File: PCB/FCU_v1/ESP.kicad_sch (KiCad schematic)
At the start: 10 parts, among them IC3 ESP32-C3-MINI-1-N4X, SW3 SW_MEC_5G

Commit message: Repaired library
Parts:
- removed IC3: ESP32-C3-MINI-1-N4X, ESP32C3MINI1N4X, symbol SamacSys_Parts:ESP32-C3-MINI-1-N4X
- added IC4: ESP32-C3-MINI-1-N4X, ESP32C3MINI1N4X, symbol SamacSys_Parts:ESP32-C3-MINI-1-N4X
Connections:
- net +3.3V: now also IC4.3 (3V3)
- net GND: now also IC4.1 (GND), IC4.11 (GND_3), IC4.14 (GND_4), IC4.2 (GND_2), IC4.36 (GND_5), IC4.37 (GND_6), IC4.38 (GND_7), IC4.39 (GND_8), IC4.40 (GND_9), IC4.41 (GND_10), IC4.42 (GND_11), IC4.43 (GND_12), IC4.44 (GND_13), IC4.45 (GND_14), IC4.46 (GND_15), IC4.47 (GND_16), IC4.48 (GND_17), IC4.49 (GND_18), IC4.50 (GND_19), IC4.51 (GND_20), IC4.52 (GND_21), IC4.53 (GND_22), IC4.54 (GND_23), IC4.55 (GND_24), IC4.56 (GND_25), IC4.57 (GND_26), IC4.58 (GND_27), IC4.59 (GND_28), IC4.60 (GND_29), IC4.61 (GND_30)
- net UART_RX_ESP_DBG: now also IC4.30 (RXD0)
- net UART_RX_ESP_STM: now also IC4.6 (IO3)
- net UART_TX_ESP_DBG: now also IC4.31 (TXD0)
- net UART_TX_ESP_STM: now also IC4.16 (IO10)
- net at C44.1, R44.1, R45.2: now also IC4.8 (EN)
- net at R46.1: now also IC4.19 (IO5)
- new net: IC4.10 (NC_4), IC4.15 (NC_5), IC4.17 (NC_6), IC4.24 (NC_7), IC4.25 (NC_8), IC4.28 (NC_9), IC4.29 (NC_10), IC4.32 (NC_11), IC4.33 (NC_12), IC4.34 (NC_13), IC4.35 (NC_14), IC4.4 (NC_1), IC4.7 (NC_2), IC4.9 (NC_3)
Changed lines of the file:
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@@
+	)
+	(symbol
+		(lib_id "SamacSys_Parts:ESP32-C3-MINI-1-N4X")
+		(at 76.2 58.42 0)
+		(unit 1)
+		(exclude_from_sim no)
+		(in_bom yes)
+		(on_board yes)
+		(dnp no)
+		(fields_autoplaced yes)
+		(property "Reference" "IC4"
+			(at 94.8533 54.61 0)
+			(effects
+				(font
+					(size 1.27 1.27)
+				)
+				(justify left)
+			)
+		)
+		(property "Value" "ESP32-C3-MINI-1-N4X"
+			(at 94.8533 57.15 0)
+			(effects
+				(font
+					(size 1.27 1.27)
+				)
+				(justify left)
+			)
+		)
+		(property "Footprint" "ESP32C3MINI1N4X"
+			(at 105.41 153.34 0)
+			(effects
+				(font
+					(size 1.27 1.27)
+				)
+				(justify left top)
+				(hide yes)
+			)
+		)
+		(property "Datasheet" "https://documentation.espressif.com/esp32-c3-mini-1_datasheet_en.pdf"
+			(at 105.41 253.34 0)
+			(effects
+				(font
+					(size 1.27 1.27)
+				)
+				(justify left top)
+				(hide yes)
+			)
+		)
+		(property "Description" "Bluetooth, WiFi 802.11b/g/n, Bluetooth v5.0 Transceiver Module 2.4GHz Integrated, Trace Surface Mount , 3V ~ 3.6V , -40C ~ 85C (TA)"
+			(at 76.2 58.42 0)
+			(effects
+				(font
+					(size 1.27 1.27)
+				)
+				(hide yes)
+			)
+		)
+		(property "Height" "2.55"
+			(at 105.41 453.34 0)
+			(effects
+				(font
+					(size 1.27 1.27)
+				)
+				(justify left top)
+				(hide yes)
+			)
+		)
+		(property "Mouser Part Number" ""
+			(at 105.41 553.34 0)
+			(effects
+				(font
+					(size 1.27 1.27)
+				)
+				(justify left top)
+				(hide yes)
+			)
+		)
+		(property "Mouser Price/Stock" ""
+			(at 105.41 653.34 0)
+			(effects
+				(font
+					(size 1.27 1.27)
+				)
+				(justify left top)
+				(hide yes)
+			)
+		)
+		(property "Manufacturer_Name" "Espressif Systems"
+			(at 105.41 753.34 0)
+			(effects
+				(font
+					(size 1.27 1.27)
+				)
+				(justify left top)
+				(hide yes)
+			)
+		)
+		(property "Manufacturer_Part_Number" "ESP32-C3-MINI-1-N4X"
+			(at 105.41 853.34 0)
+			(effects
+				(font
+					(size 1.27 1.27)
+				)
+				(justify left top)
+				(hide yes)
+			)
+		)
+		(pin "18"
+		)
+		(pin "20"
+		)
+		(pin "33"
+		)
+		(pin "13"
+		)
+		(pin "10"
+		)
+		(pin "29"
+		)
+		(pin "16"
+		)
+		(pin "14"
+		)
+		(pin "4"
+		)
+		(pin "34"
+		)
+		(pin "25"
+		)
+		(pin "24"
+		)
+		(pin "28"
+		)
+		(pin "35"
+		)
+		(pin "9"
+		)
+		(pin "6"
+		)
+		(pin "17"
+		)
+		(pin "12"
+		)
+		(pin "32"
+		)
+		(pin "5"
+		)
+		(pin "15"
+		)
+		(pin "7"
+		)
+		(pin "19"
+		)
+		(pin "21"
+		)
+		(pin "22"
+		)
+		(pin "23"
+		)
+		(pin "3"
+		)
+		(pin "1"
+		)
+		(pin "11"
+		)
+		(pin "58"
+		)
+		(pin "36"
+		)
+		(pin "61"
+		)
+		(pin "42"
+		)
+		(pin "43"
+		)
+		(pin "48"
+		)
+		(pin "40"
+		)
+		(pin "2"
+		)
+		(pin "49"
+		)
+		(pin "50"
+		)
+		(pin "37"
+		)
+		(pin "41"
+		)
+		(pin "45"
+		)
+		(pin "52"
+		)
+		(pin "53"
+		)
+		(pin "54"
+		)
+		(pin "44"
+		)
+		(pin "47"
+		)
+		(pin "55"
+		)
+		(pin "51"
+		)
+		(pin "56"
+		)
+		(pin "57"
+		)
+		(pin "39"
+		)
+		(pin "38"
+		)
+		(pin "46"
+		)
+		(pin "59"
+		)
+		(pin "60"
+		)
+		(pin "30"
+		)
+		(pin "31"
+		)
+		(pin "8"
+		)
+		(pin "26"
+		)
+		(pin "27"
+		)
+		(instances
+			(project ""
+				(path "/ace60bf5-8c2a-49e8-98f3-824f03a0dfeb/aae47d4f-fc32-408a-9d63-5fc67cfcb68c"
+					(reference "IC4")
+					(unit 1)
+				)
+			)
+		)
 	)
 	(symbol
@@
 					(unit 1)
 				)
-			)
-		)
-	)
-	(symbol
-		(lib_id "SamacSys_Parts:ESP32-C3-MINI-1-N4X")
-		(at 76.2 58.42 0)
-		(unit 1)
-		(exclude_from_sim no)
-		(in_bom yes)
-		(on_board yes)
-		(dnp no)
-		(property "Reference" "IC3"
-			(at 95.504 57.912 0)
-			(effects
-				(font
-					(size 1.27 1.27)
-				)
-				(justify left)
-			)
-		)
-		(property "Value" "ESP32-C3-MINI-1-N4X"
-			(at 93.98 95.25 0)
-			(effects
-				(font
-					(size 1.27 1.27)
-				)
-				(justify left)
-			)
-		)
-		(property "Footprint" "ESP32C3MINI1N4X"
-			(at 105.41 153.34 0)
-			(effects
-				(font
-					(size 1.27 1.27)
-				)
-				(justify left top)
-				(hide yes)
-			)
-		)
-		(property "Datasheet" "https://documentation.espressif.com/esp32-c3-mini-1_datasheet_en.pdf"
-			(at 105.41 253.34 0)
-			(effects
-				(font
-					(size 1.27 1.27)
-				)
-				(justify left top)
-				(hide yes)
-			)
-		)
-		(property "Description" "Bluetooth, WiFi 802.11b/g/n, Bluetooth v5.0 Transceiver Module 2.4GHz Integrated, Trace Surface Mount , 3V ~ 3.6V , -40C ~ 85C (TA)"
-			(at 76.2 58.42 0)
-			(effects
-				(font
-					(size 1.27 1.27)
-				)
-				(hide yes)
-			)
-		)
-		(property "Height" "2.55"
-			(at 105.41 453.34 0)
-			(effects
-				(font
-					(size 1.27 1.27)
-				)
-				(justify left top)
-				(hide yes)
-			)
-		)
-		(property "Mouser Part Number" ""
-			(at 105.41 553.34 0)
-			(effects
-				(font
-					(size 1.27 1.27)
-				)
-				(justify left top)
-				(hide yes)
-			)
-		)
-		(property "Mouser Price/Stock" ""
-			(at 105.41 653.34 0)
-			(effects
-				(font
-					(size 1.27 1.27)
-				)
-				(justify left top)
-				(hide yes)
-			)
-		)
-		(property "Manufacturer_Name" "Espressif Systems"
-			(at 105.41 753.34 0)
-			(effects
-				(font
-					(size 1.27 1.27)
-				)
-				(justify left top)
-				(hide yes)
-			)
-		)
-		(property "Manufacturer_Part_Number" "ESP32-C3-MINI-1-N4X"
-			(at 105.41 853.34 0)
-			(effects
-				(font
-					(size 1.27 1.27)
-				)
-				(justify left top)
-				(hide yes)
-			)
-		)
-		(pin "14"
-		)
-		(pin "2"
-		)
-		(pin "21"
-		)
-		(pin "16"
-		)
-		(pin "26"
-		)
-		(pin "28"
-		)
-		(pin "15"
-		)
-		(pin "7"
-		)
-		(pin "10"
-		)
-		(pin "1"
-		)
-		(pin "3"
-		)
-		(pin "5"
-		)
-		(pin "6"
-		)
-		(pin "9"
-		)
-		(pin "11"
-		)
-		(pin "8"
-		)
-		(pin "4"
-		)
-		(pin "12"
-		)
-		(pin "13"
-		)
-		(pin "18"
-		)
-		(pin "17"
-		)
-		(pin "19"
-		)
-		(pin "20"
-		)
-		(pin "22"
-		)
-		(pin "23"
-		)
-		(pin "24"
-		)
-		(pin "25"
-		)
-		(pin "27"
-		)
-		(pin "53"
-		)
-		(pin "50"
-		)
-		(pin "31"
-		)
-		(pin "40"
-		)
-		(pin "47"
-		)
-		(pin "37"
-		)
-		(pin "34"
-		)
-		(pin "42"
-		)
-		(pin "46"
-		)
-		(pin "32"
-		)
-		(pin "33"
-		)
-		(pin "35"
-		)
-		(pin "45"
-		)
-		(pin "44"
-		)
-		(pin "49"
-		)
-		(pin "52"
-		)
-		(pin "48"
-		)
-		(pin "39"
-		)
-		(pin "30"
-		)
-		(pin "41"
-		)
-		(pin "29"
-		)
-		(pin "38"
-		)
-		(pin "43"
-		)
-		(pin "36"
-		)
-		(pin "51"
-		)
-		(pin "54"
-		)
-		(pin "56"
-		)
-		(pin "57"
-		)
-		(pin "55"
-		)
-		(pin "61"
-		)
-		(pin "58"
-		)
-		(pin "59"
-		)
-		(pin "60"
-		)
-		(instances
-			(project "FCU_v1"
-				(path "/ace60bf5-8c2a-49e8-98f3-824f03a0dfeb/aae47d4f-fc32-408a-9d63-5fc67cfcb68c"
-					(reference "IC3")
-					(unit 1)
-				)

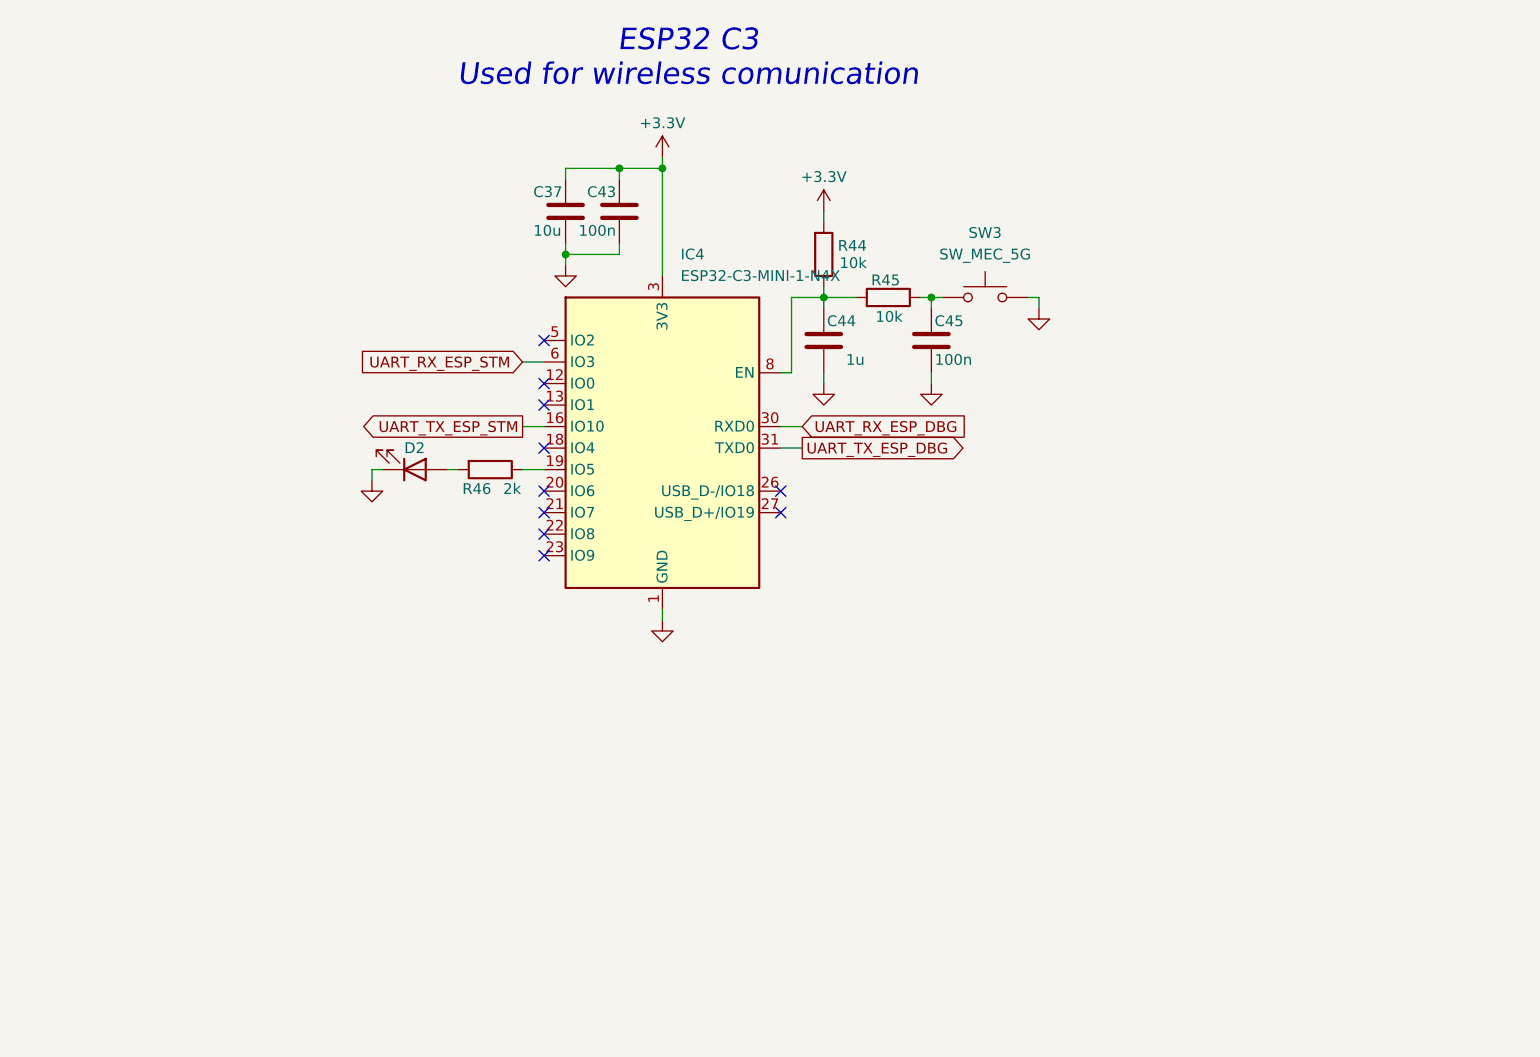
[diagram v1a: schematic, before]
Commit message: Components change and layout update
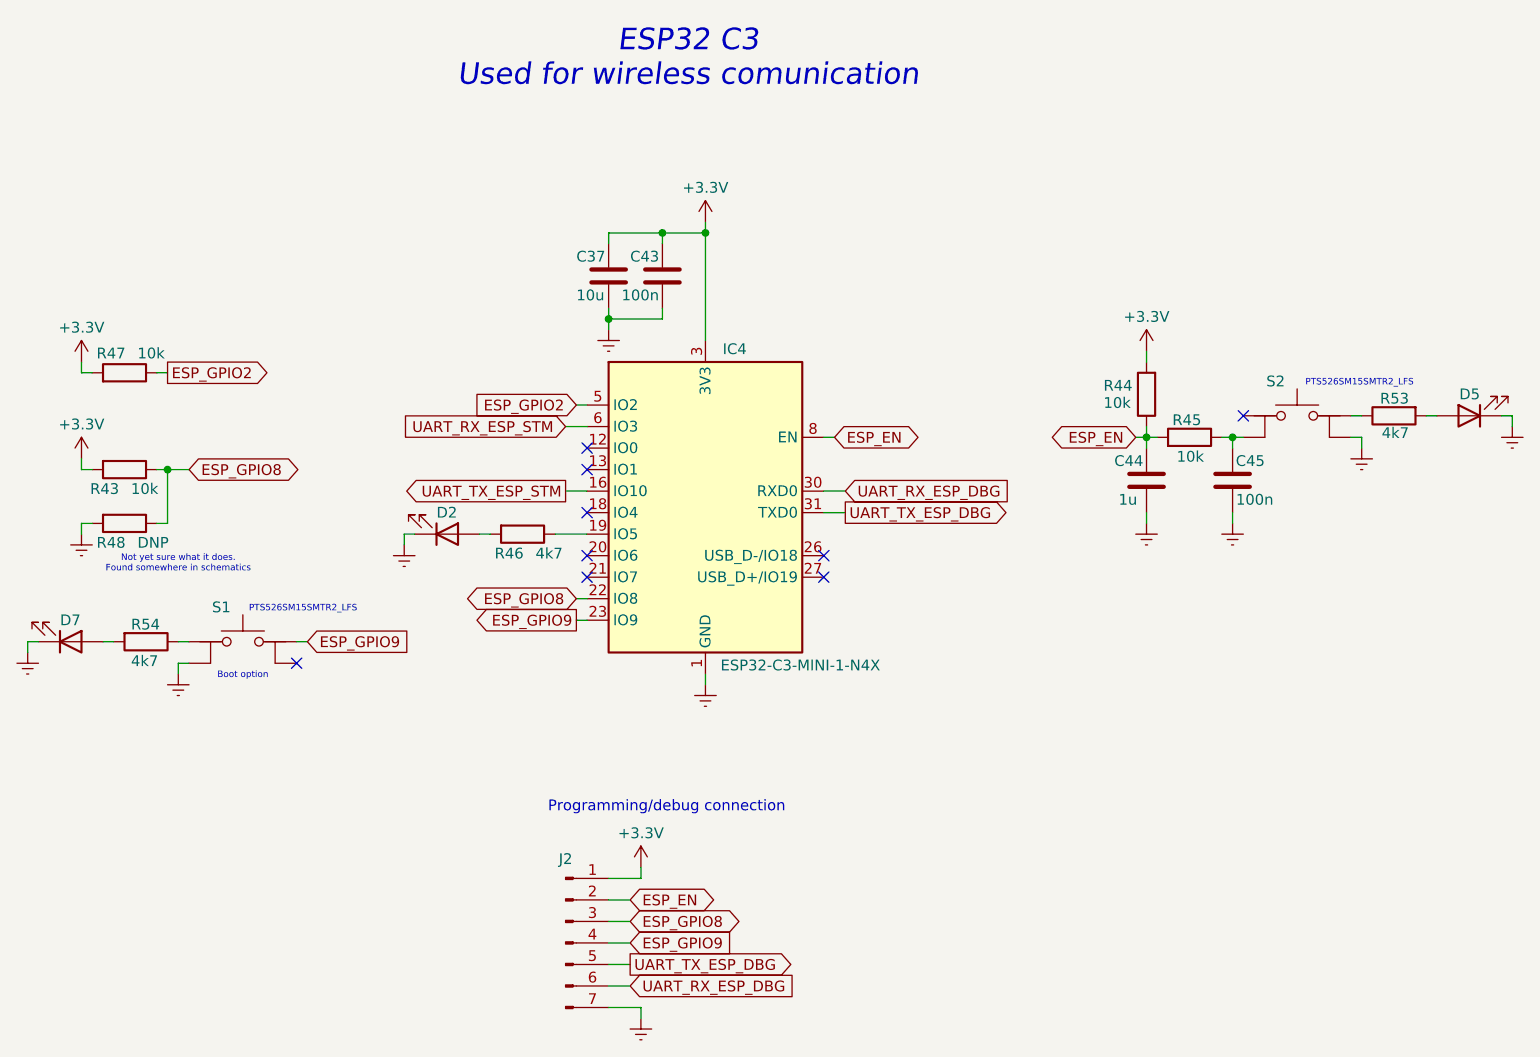
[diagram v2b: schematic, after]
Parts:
- removed SW3: SW_MEC_5G, Button_Switch_SMD:SW_MEC_5GSH9, symbol Switch:SW_MEC_5G
- added D5, D7: LED, LED_SMD:LED_0805_2012Metric, symbol Device:LED
- added J2: Conn_01x07_Pin, Connector_PinHeader_2.54mm:PinHeader_1x07_P2.54mm_Vertical, symbol Connector:Conn_01x07_Pin
- added R43, R47: 10k, Resistor_SMD:R_0603_1608Metric, symbol Device:R
- added R48: DNP, Resistor_SMD:R_0201_0603Metric, symbol Device:R
- added R53, R54: 4k7, Resistor_SMD:R_0603_1608Metric, symbol Device:R
- added S1, S2: PTS526SM15SMTR2_LFS, PTS526SM15SMTR2LFS, symbol SamacSys_Parts:PTS526SM15SMTR2_LFS
- R46: value 2k -> 4k7
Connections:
- net +3.3V: now also J2.1 (Pin_1), R43.2, R47.2
- net GND: now also D5.1 (K), D7.1 (K), J2.7 (Pin_7), R48.2, S1.2 (COM_2), S2.4 (NO_2)
- net UART_RX_ESP_DBG: now also J2.6 (Pin_6)
- net UART_TX_ESP_DBG: now also J2.5 (Pin_5)
- net at C45.1, R45.1: now also S2.2 (COM_2)
- net ESP_EN: now reaches C44.1, IC4.8 (EN), R44.1, R45.2
- net ESP_EN: now also J2.2 (Pin_2)
- net ESP_GPIO8: now reaches IC4.22 (IO8)
- net ESP_GPIO8: now also J2.3 (Pin_3), R43.1, R48.1
- net ESP_GPIO9: now reaches IC4.23 (IO9)
- net ESP_GPIO9: now also J2.4 (Pin_4), S1.3 (NO_1)
- net ESP_GPIO2: now reaches IC4.5 (IO2)
- net ESP_GPIO2: now also R47.1
- new net: R53.1, S2.3 (NO_1)
- new net: D7.2 (A), R54.2
- new net: R54.1, S1.1 (COM_1)
- new net: D5.2 (A), R53.2
- no-connect marks 10 -> 9
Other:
- note added: "Boot option"
- note added: "Not yet sure what it does. Found somewhere in schematics"
- note added: "PTS526SM15SMTR2_LFS"
- note added: "Programming/debug connection"
- moved on the sheet: C37, C43, C44, C45, D2, IC4, R44, R45, R46

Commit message: Layout update
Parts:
- removed IC4: ESP32-C3-MINI-1-N4X, ESP32C3MINI1N4X, symbol SamacSys_Parts:ESP32-C3-MINI-1-N4X
- removed J2: Conn_01x07_Pin, Connector_PinHeader_2.54mm:PinHeader_1x07_P2.54mm_Vertical, symbol Connector:Conn_01x07_Pin
- removed S1: PTS526SM15SMTR2_LFS, PTS526SM15SMTR2LFS, symbol SamacSys_Parts:PTS526SM15SMTR2_LFS
- added IC3: ESP32-C3-MINI-1-N4X, ESP32C3MINI1N4X, symbol SamacSys_Parts:ESP32-C3-MINI-1-N4X
- added J14, J15, J16: Conn_01x02_Pin, Connector_PinHeader_2.54mm:PinHeader_1x02_P2.54mm_Vertical, symbol Connector:Conn_01x02_Pin
- added J17: Conn_01x01_Pin, Connector_PinHeader_2.54mm:PinHeader_1x01_P2.54mm_Vertical, symbol Connector:Conn_01x01_Pin
- added R38: 4k7, Resistor_SMD:R_0603_1608Metric, symbol Device:R
- added S3: PTS526SM15SMTR2_LFS, PTS526SM15SMTR2LFS, symbol SamacSys_Parts:PTS526SM15SMTR2_LFS
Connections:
- net +3.3V: now also IC3.3 (3V3), J14.1 (Pin_1)
- net ESP_EN: now also IC3.8 (EN), J17.1 (Pin_1)
- net ESP_GPIO2: now also IC3.5 (IO2)
- net ESP_GPIO8: now also IC3.22 (IO8), J16.1 (Pin_1)
- net ESP_GPIO9: now also IC3.23 (IO9), J16.2 (Pin_2), S3.3 (NO_1)
- net GND: now also IC3.1 (GND), IC3.11 (GND_3), IC3.14 (GND_4), IC3.2 (GND_2), IC3.36 (GND_5), IC3.37 (GND_6), IC3.38 (GND_7), IC3.39 (GND_8), IC3.40 (GND_9), IC3.41 (GND_10), IC3.42 (GND_11), IC3.43 (GND_12), IC3.44 (GND_13), IC3.45 (GND_14), IC3.46 (GND_15), IC3.47 (GND_16), IC3.48 (GND_17), IC3.49 (GND_18), IC3.50 (GND_19), IC3.51 (GND_20), IC3.52 (GND_21), IC3.53 (GND_22), IC3.54 (GND_23), IC3.55 (GND_24), IC3.56 (GND_25), IC3.57 (GND_26), IC3.58 (GND_27), IC3.59 (GND_28), IC3.60 (GND_29), IC3.61 (GND_30), J14.2 (Pin_2), S3.2 (COM_2)
- net UART_RX_ESP_DBG: now also IC3.30 (RXD0), J15.2 (Pin_2)
- net UART_TX_ESP_DBG: now also IC3.31 (TXD0), J15.1 (Pin_1)
- net at R46.1: now also IC3.19 (IO5)
- net at R54.1: now also S3.1 (COM_1)
- new net: IC3.10 (NC_4), IC3.15 (NC_5), IC3.17 (NC_6), IC3.24 (NC_7), IC3.25 (NC_8), IC3.28 (NC_9), IC3.29 (NC_10), IC3.32 (NC_11), IC3.33 (NC_12), IC3.34 (NC_13), IC3.35 (NC_14), IC3.4 (NC_1), IC3.7 (NC_2), IC3.9 (NC_3)
- new net USART2_RX: R38.2
- new net USART2_RX_ESP: IC3.18 (IO4), R38.1
- new net USART2_TX: IC3.16 (IO10)
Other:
- moved on the sheet: D2, R43, R46, R48

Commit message: Layout update
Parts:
- C43: footprint Capacitor_SMD:C_0805_2012Metric -> Capacitor_SMD:C_0603_1608Metric
- R48: footprint Resistor_SMD:R_0201_0603Metric -> Resistor_SMD:R_0402_1005Metric
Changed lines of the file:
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@@
 	(text "Programming/debug connection"
 		(exclude_from_sim no)
-		(at 93.218 114.808 0)
+		(at 74.168 122.428 0)
 		(effects
 			(font
@@
 			)
 		)
-		(property "Footprint" "Capacitor_SMD:C_0805_2012Metric"
+		(property "Footprint" "Capacitor_SMD:C_0603_1608Metric"
 			(at 93.6752 60.96 0)
 			(effects
@@
 			)
 		)
-		(property "Footprint" "Resistor_SMD:R_0201_0603Metric"
+		(property "Footprint" "Resistor_SMD:R_0402_1005Metric"
 			(at 29.21 82.042 90)
 			(effects
